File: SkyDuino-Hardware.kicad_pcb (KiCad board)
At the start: 4 copper layers, 123 x 56 mm, 83 parts, among them J1 24V, J11 DBG, J12 USB-A RMT, J13 DISP, J14 USB_C Artisan, J2 BT, J4 Drum, J5 Exhaust, J6 Cooling, J7 Cooling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

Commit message: Remove LSE from PCB
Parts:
- removed C26, C27: 7.5pF, Capacitor_SMD:C_0805_2012Metric_Pad1.18x1.45mm_HandSolder
- removed Y1: 32.768kHz, Oscillators:Diodes Inc G43270021
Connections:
- U9 pad 3: /CPU/XTAL_32K768_1 -> unconnected-(U9-PC14-Pad3)
- U9 pad 4: /CPU/XTAL_32K768_2 -> unconnected-(U9-PC15-Pad4)
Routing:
- net /CPU/XTAL_32K768_1: track 12.7 -> 0.00 mm
- net /CPU/XTAL_32K768_2: track 11.1 -> 0.00 mm

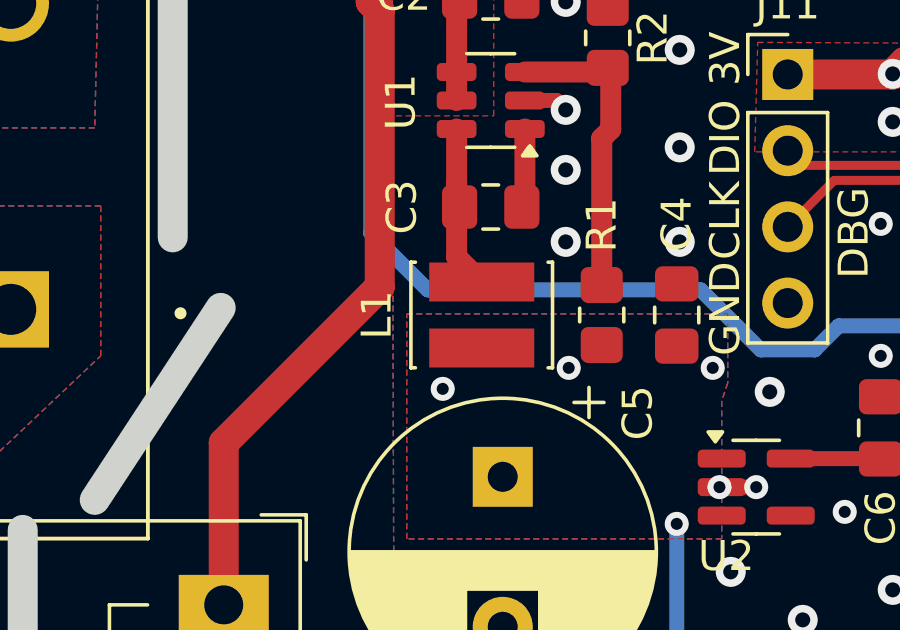
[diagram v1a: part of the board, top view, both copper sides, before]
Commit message: Replace L1 with Sunlord SWPA4030S180MT
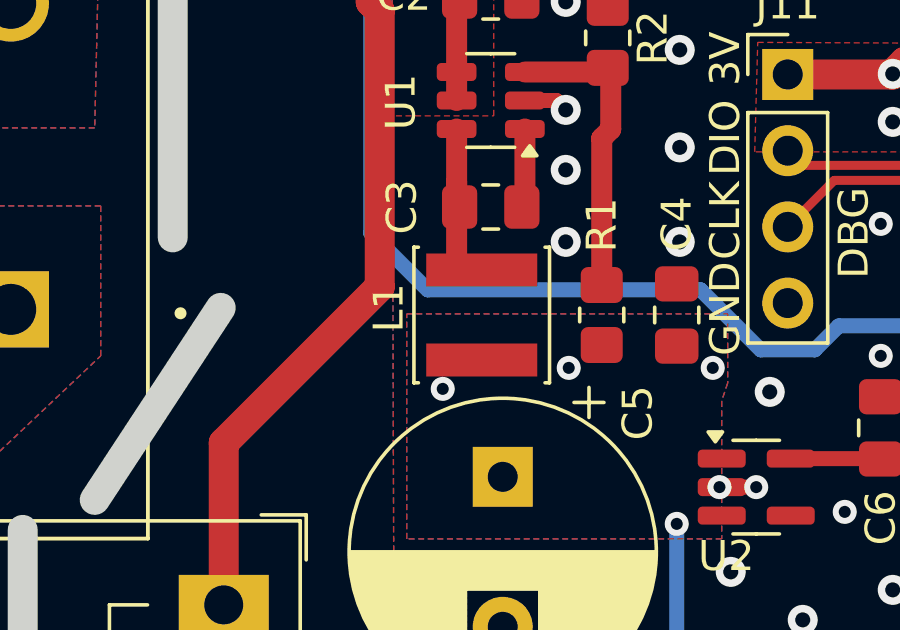
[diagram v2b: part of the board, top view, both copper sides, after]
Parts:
- L1: footprint Inductor_Bourns:L_Bourns_SRN3015BTA -> Inductor_SMD:L_Sunlord_SWPA4030S
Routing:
- net Net-(U1-SW): track 6.40 -> 5.21 mm
